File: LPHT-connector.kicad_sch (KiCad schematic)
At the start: 1 part, among them J2 LPHT-04-16-L-RT1-GP

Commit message: minor changes/cleanup
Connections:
- net ET1: now reaches J2.09
- net ET2: now reaches J2.10
- net ET3: now reaches J2.11
- net ET4: now reaches J2.12
- net ET5: now reaches J2.13
- net ET6: now reaches J2.14
- net ET7: now reaches J2.15
- net ET8: now reaches J2.16
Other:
- note added: "This needs to be an "LPHS-04-16-L-VP1""
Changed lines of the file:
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@@
 	(text "9-16 lan\n"
 		(exclude_from_sim no)
-		(at 170.434 85.598 0)
+		(at 182.88 86.106 0)
+		(effects
+			(font
+				(size 1.27 1.27)
+			)
+		)
+	)
+	(text "This needs to be an \"LPHS-04-16-L-VP1\""
+		(exclude_from_sim no)
+		(at 149.86 61.976 0)
 		(effects
 			(font
@@
 	(wire
 		(pts
+			(xy 163.83 85.09) (xy 171.45 85.09)
+		)
+		(stroke
+			(width 0)
+			(type default)
+		)
+	)
+	(wire
+		(pts
 			(xy 138.43 107.95) (xy 138.43 110.49)
 		)
@@
 	(wire
 		(pts
+			(xy 163.83 95.25) (xy 171.45 95.25)
+		)
+		(stroke
+			(width 0)
+			(type default)
+		)
+	)
+	(wire
+		(pts
 			(xy 163.83 115.57) (xy 163.83 118.11)
 		)
@@
 	(wire
 		(pts
+			(xy 163.83 87.63) (xy 171.45 87.63)
+		)
+		(stroke
+			(width 0)
+			(type default)
+		)
+	)
+	(wire
+		(pts
 			(xy 163.83 118.11) (xy 163.83 120.65)
 		)
@@
 	(wire
 		(pts
+			(xy 163.83 90.17) (xy 171.45 90.17)
+		)
+		(stroke
+			(width 0)
+			(type default)
+		)
+	)
+	(wire
+		(pts
 			(xy 127 85.09) (xy 138.43 85.09)
 		)
@@
 	(wire
 		(pts
+			(xy 163.83 77.47) (xy 171.45 77.47)
+		)
+		(stroke
+			(width 0)
+			(type default)
+		)
+	)
+	(wire
+		(pts
 			(xy 138.43 105.41) (xy 138.43 107.95)
 		)
@@
 	(wire
 		(pts
+			(xy 163.83 92.71) (xy 171.45 92.71)
+		)
+		(stroke
+			(width 0)
+			(type default)
+		)
+	)
+	(wire
+		(pts
 			(xy 127 78.74) (xy 138.43 78.74)
 		)
@@
 		(pts
 			(xy 138.43 77.47) (xy 138.43 78.74)
+		)
+		(stroke
+			(width 0)
+			(type default)
+		)
+	)
+	(wire
+		(pts
+			(xy 163.83 82.55) (xy 171.45 82.55)
+		)
+		(stroke
+			(width 0)
+			(type default)
+		)
+	)
+	(wire
+		(pts
+			(xy 163.83 80.01) (xy 171.45 80.01)
 		)
 		(stroke
@@
 		)
 	)
+	(hierarchical_label "ET1"
+		(shape input)
+		(at 171.45 77.47 0)
+		(effects
+			(font
+				(size 1.27 1.27)
+			)
+			(justify left)
+		)
+	)
+	(hierarchical_label "ET4"
+		(shape input)
+		(at 171.45 85.09 0)
+		(effects
+			(font
+				(size 1.27 1.27)
+			)
+			(justify left)
+		)
+	)
+	(hierarchical_label "ET5"
+		(shape input)
+		(at 171.45 87.63 0)
+		(effects
+			(font
+				(size 1.27 1.27)
+			)
+			(justify left)
+		)
+	)
+	(hierarchical_label "ET2"
+		(shape input)
+		(at 171.45 80.01 0)
+		(effects
+			(font
+				(size 1.27 1.27)
+			)
+			(justify left)
+		)
+	)
+	(hierarchical_label "ET8"
+		(shape input)
+		(at 171.45 95.25 0)
+		(effects
+			(font
+				(size 1.27 1.27)
+			)
+			(justify left)
+		)
+	)
+	(hierarchical_label "ET6"
+		(shape input)
+		(at 171.45 90.17 0)
+		(effects
+			(font
+				(size 1.27 1.27)
+			)
+			(justify left)
+		)
+	)
+	(hierarchical_label "ET7"
+		(shape input)
+		(at 171.45 92.71 0)
+		(effects
+			(font
+				(size 1.27 1.27)
+			)
+			(justify left)
+		)
+	)
+	(hierarchical_label "ET3"
+		(shape input)
+		(at 171.45 82.55 0)
+		(effects
+			(font
+				(size 1.27 1.27)
+			)
+			(justify left)
+		)
+	)

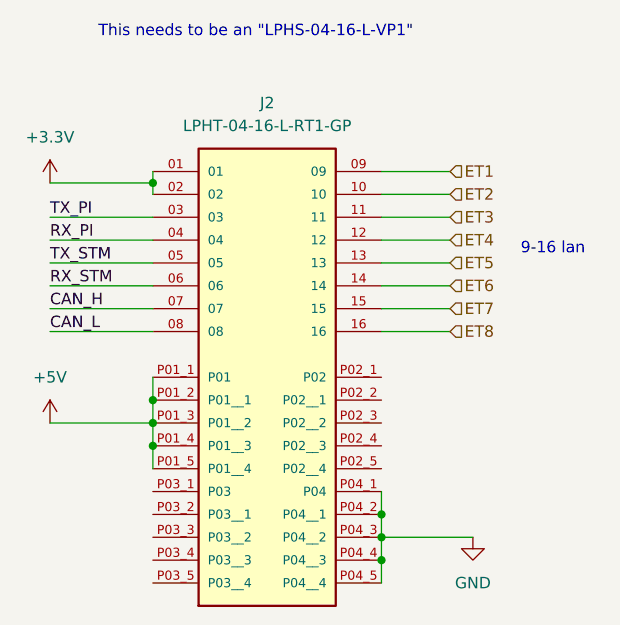
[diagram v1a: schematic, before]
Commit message: Added usb connector
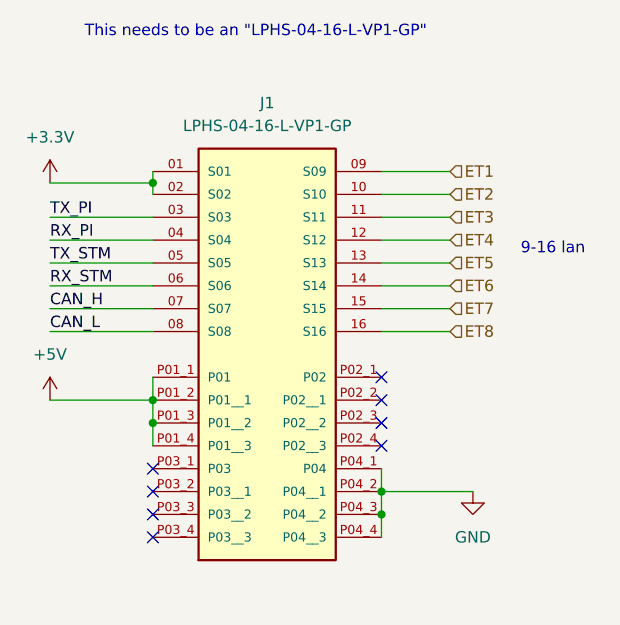
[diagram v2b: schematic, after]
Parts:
- removed J2: LPHT-04-16-L-RT1-GP, dz_con:SAMTEC_LPHT-04-16-X-RT1-GP, symbol #dzdb:s_con/CON-SAMTEC-LPHT-04-16-L-RT1-GP
- added J1: LPHS-04-16-L-VP1-GP, dz_con:SAMTEC_LPHS-04-16-X-VP1-GP, symbol #dzdb:s_con/CON-SAMTEC-LPHS-04-16-L-VP1-GP
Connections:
- net +3.3V: now also J1.01 (S01), J1.02 (S02)
- net +5V: now also J1.P01_1 (P01), J1.P01_2 (P01__1), J1.P01_3 (P01__2), J1.P01_4 (P01__3)
- net CAN_H: now also J1.07 (S07)
- net CAN_L: now also J1.08 (S08)
- net ET1: now also J1.09 (S09)
- net ET2: now also J1.10 (S10)
- net ET3: now also J1.11 (S11)
- net ET4: now also J1.12 (S12)
- net ET5: now also J1.13 (S13)
- net ET6: now also J1.14 (S14)
- net ET7: now also J1.15 (S15)
- net ET8: now also J1.16 (S16)
- net GND: now also J1.P04_1 (P04), J1.P04_2 (P04__1), J1.P04_3 (P04__2), J1.P04_4 (P04__3)
- net RX_PI: now also J1.04 (S04)
- net RX_STM: now also J1.06 (S06)
- net TX_PI: now also J1.03 (S03)
- net TX_STM: now also J1.05 (S05)
- no-connect marks 0 -> 8
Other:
- note added: "This needs to be an "LPHS-04-16-L-VP1-GP""
- note removed: "This needs to be an "LPHS-04-16-L-VP1""

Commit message: Comments (+ new Connector?)
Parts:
- added J3: LPHT-04-16-L-RT1-GP, dz_con:SAMTEC_LPHT-04-16-X-RT1-GP, symbol #dzdb:s_con/CON-SAMTEC-LPHT-04-16-L-RT1-GP
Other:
- note added: "3.3 not needed?"

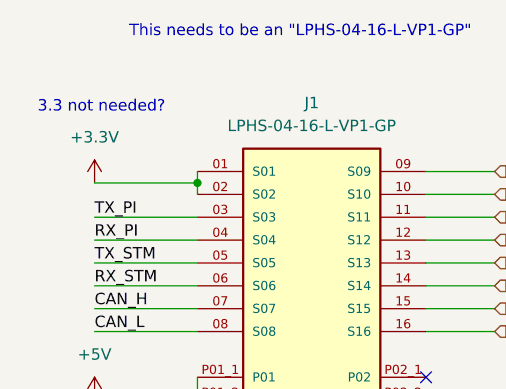
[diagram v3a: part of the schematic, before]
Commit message: multiple changes. fixed some mistakes, added jumper pins for wifi
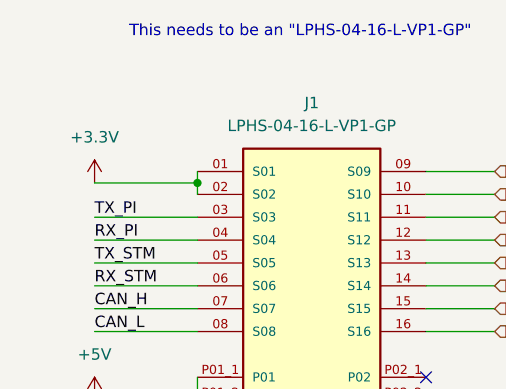
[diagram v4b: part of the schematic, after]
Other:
- note removed: "3.3 not needed?"
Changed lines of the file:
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@@
-		)
-	)
-	(text "3.3 not needed?\n"
-		(exclude_from_sim no)
-		(at 127.762 70.358 0)
-		(effects
-			(font
-				(size 1.27 1.27)
-			)
 		)
 	)

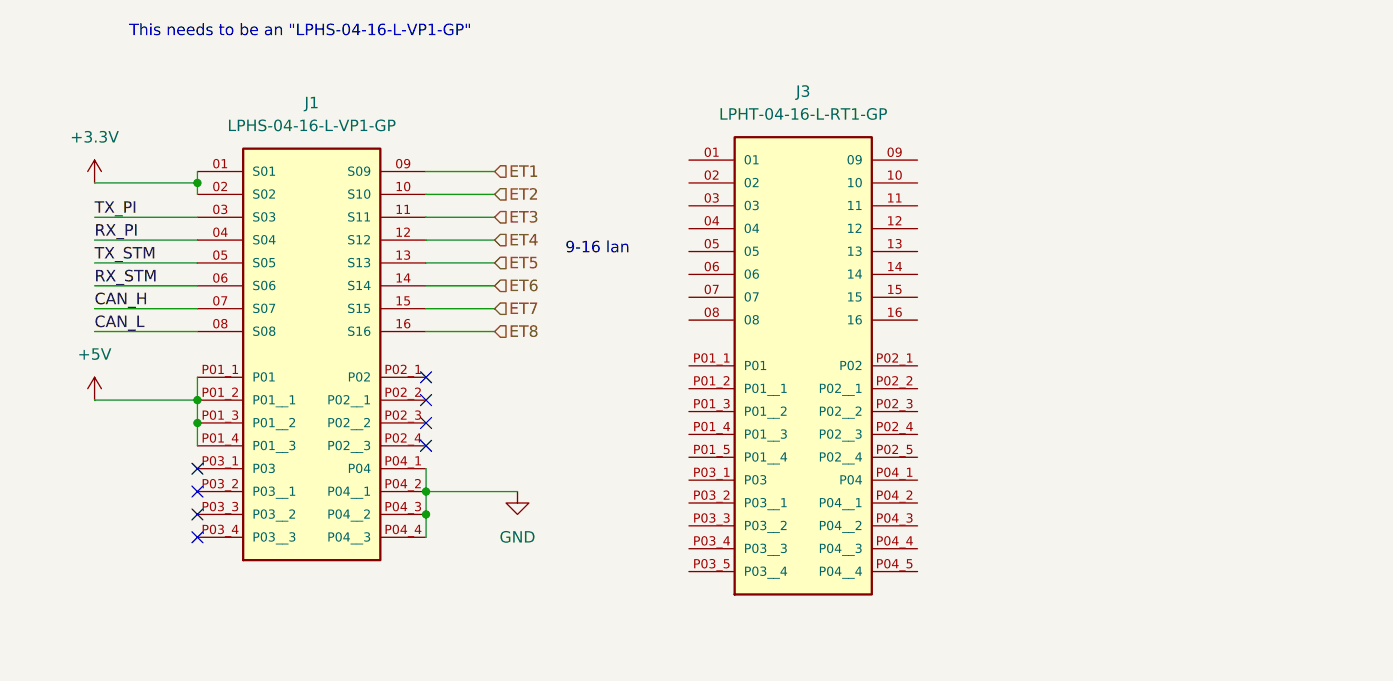
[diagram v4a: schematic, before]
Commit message: connector changes
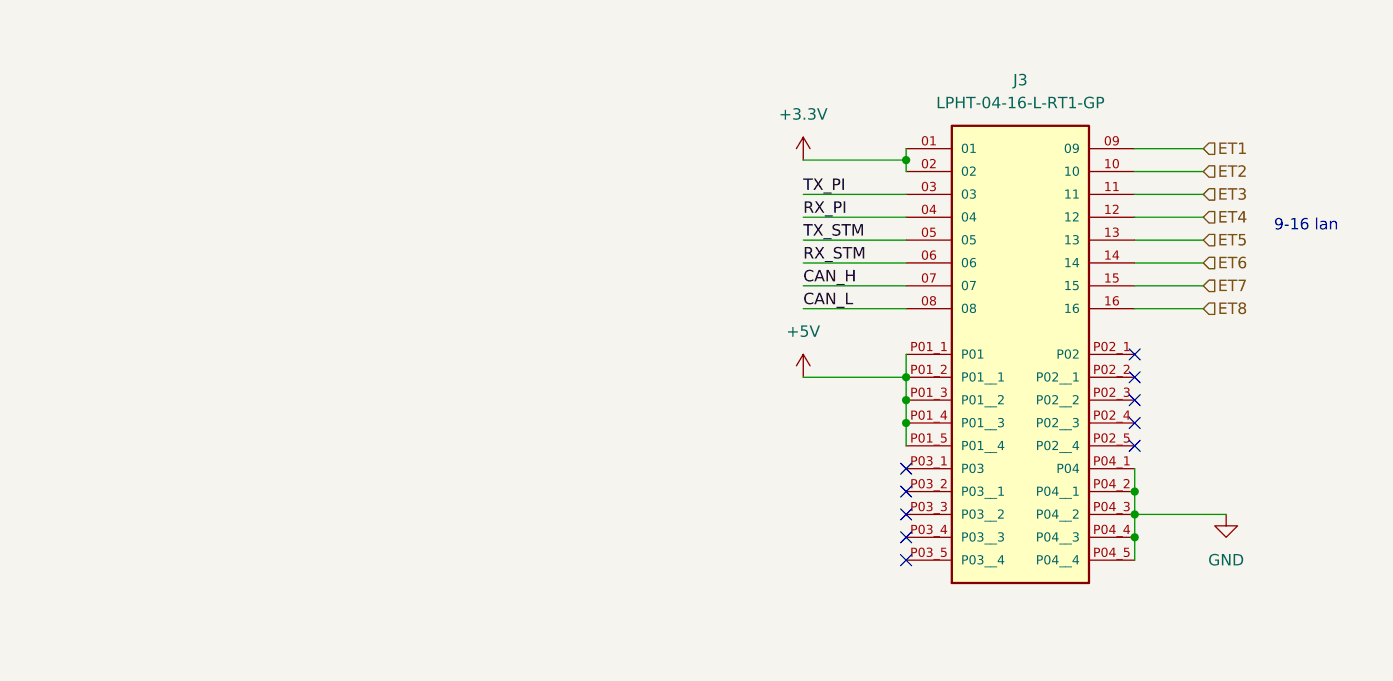
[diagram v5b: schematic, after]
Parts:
- removed J1: LPHS-04-16-L-VP1-GP, dz_con:SAMTEC_LPHS-04-16-X-VP1-GP, symbol #dzdb:s_con/CON-SAMTEC-LPHS-04-16-L-VP1-GP
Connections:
- net +3.3V: now also J3.01, J3.02
- net +5V: now also J3.P01_1 (P01), J3.P01_2 (P01__1), J3.P01_3 (P01__2), J3.P01_4 (P01__3), J3.P01_5 (P01__4)
- net CAN_H: now also J3.07
- net CAN_L: now also J3.08
- net ET1: now also J3.09
- net ET2: now also J3.10
- net ET3: now also J3.11
- net ET4: now also J3.12
- net ET5: now also J3.13
- net ET6: now also J3.14
- net ET7: now also J3.15
- net ET8: now also J3.16
- net GND: now also J3.P04_1 (P04), J3.P04_2 (P04__1), J3.P04_3 (P04__2), J3.P04_4 (P04__3), J3.P04_5 (P04__4)
- net RX_PI: now also J3.04
- net RX_STM: now also J3.06
- net TX_PI: now also J3.03
- net TX_STM: now also J3.05
- no-connect marks 8 -> 10
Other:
- note removed: "This needs to be an "LPHS-04-16-L-VP1-GP""
- moved on the sheet: J3

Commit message: Added Power logic finally. (plus some comments on further improvements)
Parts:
- renumbered J3 to J7
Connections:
- net +3.3V renamed Battery_Out_3.3V
- net +5V renamed Battery_Out_5V
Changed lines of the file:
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@@
+		)
+	)
+	(global_label "Battery_Out_3.3V"
+		(shape output)
+		(at 205.74 76.2 180)
+		(fields_autoplaced yes)
+		(effects
+			(font
+				(size 1.27 1.27)
+			)
+			(justify right)
+		)
+		(property "Intersheetrefs" "${INTERSHEET_REFS}"
+			(at 186.7892 76.2 0)
+			(effects
+				(font
+					(size 1.27 1.27)
+				)
+				(justify right)
+				(hide yes)
+			)
+		)
+	)
+	(global_label "Battery_Out_5V"
+		(shape output)
+		(at 205.74 100.33 180)
+		(fields_autoplaced yes)
+		(effects
+			(font
+				(size 1.27 1.27)
+			)
+			(justify right)
+		)
+		(property "Intersheetrefs" "${INTERSHEET_REFS}"
+			(at 188.6035 100.33 0)
+			(effects
+				(font
+					(size 1.27 1.27)
+				)
+				(justify right)
+				(hide yes)
+			)
 		)
 	)
@@
 			)
 			(justify left)
-		)
-	)
-	(symbol
-		(lib_id "power:+5V")
-		(at 205.74 100.33 0)
-		(unit 1)
-		(exclude_from_sim no)
-		(in_bom yes)
-		(on_board yes)
-		(dnp no)
-		(fields_autoplaced yes)
-		(property "Reference" "#PWR035"
-			(at 205.74 104.14 0)
-			(effects
-				(font
-					(size 1.27 1.27)
-				)
-				(hide yes)
-			)
-		)
-		(property "Value" "+5V"
-			(at 205.74 95.25 0)
-			(effects
-				(font
-					(size 1.27 1.27)
-				)
-			)
-		)
-		(property "Footprint" ""
-			(at 205.74 100.33 0)
-			(effects
-				(font
-					(size 1.27 1.27)
-				)
-				(hide yes)
-			)
-		)
-		(property "Datasheet" ""
-			(at 205.74 100.33 0)
-			(effects
-				(font
-					(size 1.27 1.27)
-				)
-				(hide yes)
-			)
-		)
-		(property "Description" "Power symbol creates a global label with name \"+5V\""
-			(at 205.74 100.33 0)
-			(effects
-				(font
-					(size 1.27 1.27)
-				)
-				(hide yes)
-			)
-		)
-		(pin "1"
-		)
-		(instances
-			(project "nautilus_mainboard"
-				(path "/ce1819b2-f280-40ed-834f-6fe4d12f809d/8ca810bd-6311-4873-a4c4-10e0b1989f7a"
-					(reference "#PWR035")
-					(unit 1)
-				)
-			)
 		)
 	)
@@
 		(dnp no)
 		(fields_autoplaced yes)
-		(property "Reference" "#PWR036"
+		(property "Reference" "#PWR029"
 			(at 252.73 121.92 0)
 			(effects
@@
 			(project "nautilus_mainboard"
 				(path "/ce1819b2-f280-40ed-834f-6fe4d12f809d/8ca810bd-6311-4873-a4c4-10e0b1989f7a"
-					(reference "#PWR036")
-					(unit 1)
-				)
-			)
-		)
-	)
-	(symbol
-		(lib_id "power:+3.3V")
-		(at 205.74 76.2 0)
-		(unit 1)
-		(exclude_from_sim no)
-		(in_bom yes)
-		(on_board yes)
-		(dnp no)
-		(fields_autoplaced yes)
-		(property "Reference" "#PWR034"
-			(at 205.74 80.01 0)
-			(effects
-				(font
-					(size 1.27 1.27)
-				)
-				(hide yes)
-			)
-		)
-		(property "Value" "+3.3V"
-			(at 205.74 71.12 0)
-			(effects
-				(font
-					(size 1.27 1.27)
-				)
-			)
-		)
-		(property "Footprint" ""
-			(at 205.74 76.2 0)
-			(effects
-				(font
-					(size 1.27 1.27)
-				)
-				(hide yes)
-			)
-		)
-		(property "Datasheet" ""
-			(at 205.74 76.2 0)
-			(effects
-				(font
-					(size 1.27 1.27)
-				)
-				(hide yes)
-			)
-		)
-		(property "Description" "Power symbol creates a global label with name \"+3.3V\""
-			(at 205.74 76.2 0)
-			(effects
-				(font
-					(size 1.27 1.27)
-				)
-				(hide yes)
-			)
-		)
-		(pin "1"
-		)
-		(instances
-			(project "nautilus_mainboard"
-				(path "/ce1819b2-f280-40ed-834f-6fe4d12f809d/8ca810bd-6311-4873-a4c4-10e0b1989f7a"
-					(reference "#PWR034")
+					(reference "#PWR029")
 					(unit 1)
 				)
@@
 		(dnp no)
 		(fields_autoplaced yes)
-		(property "Reference" "J3"
+		(property "Reference" "J7"
 			(at 229.87 67.31 0)
 			(effects
@@
 			(project ""
 				(path "/ce1819b2-f280-40ed-834f-6fe4d12f809d/8ca810bd-6311-4873-a4c4-10e0b1989f7a"
-					(reference "J3")
+					(reference "J7")
 					(unit 1)
 				)

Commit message: tried to find some placements for power routing
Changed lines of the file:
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@@
+		)
+	)
+	(text_box "Counterpiece to  LPHS-04-16-L-VP1-GP"
+		(exclude_from_sim no)
+		(at 185.42 60.96 0)
+		(size 83.82 71.12)
+		(margins 0.9525 0.9525 0.9525 0.9525)
+		(stroke
+			(width 0)
+			(type solid)
+		)
+		(fill
+			(type none)
+		)
+		(effects
+			(font
+				(size 1.27 1.27)
+			)
+			(justify left top)
 		)
 	)
@@
 	)
 	(image
-		(at 154.94 96.52)
+		(at 139.7 91.44)
 		(scale 0.431936)
 		(data "iVBORw0KGgoAAAANSUhEUgAAAhEAAANTCAIAAACfG9iWAAAAA3NCSVQICAjb4U/gAAAACXBIWXMA"

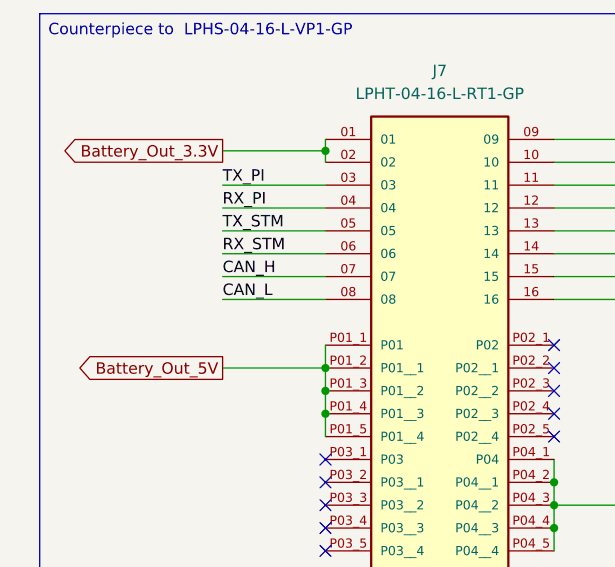
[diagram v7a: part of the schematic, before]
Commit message: routed the CAN
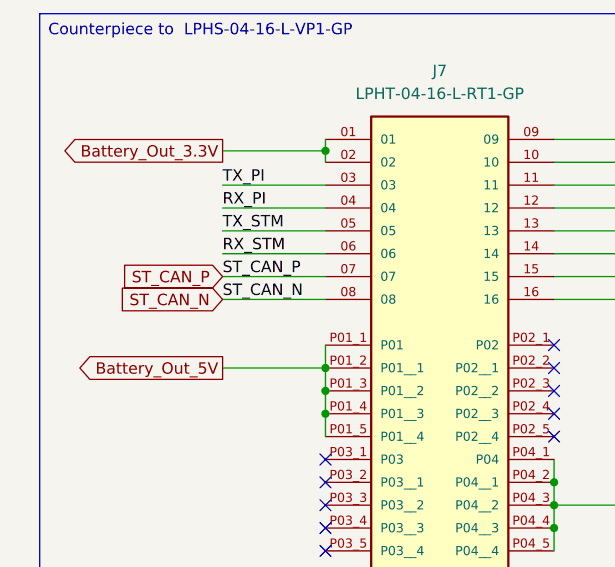
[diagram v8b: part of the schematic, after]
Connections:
- net CAN_H renamed ST_CAN_P
- net CAN_L renamed ST_CAN_N
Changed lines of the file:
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@@
 		)
 	)
-	(label "CAN_H"
+	(label "ST_CAN_P"
 		(at 205.74 90.17 0)
 		(effects
@@
 		)
 	)
-	(label "CAN_L"
+	(label "ST_CAN_N"
 		(at 205.74 92.71 0)
 		(effects
@@
 		)
 	)
+	(global_label "ST_CAN_N"
+		(shape input)
+		(at 205.74 92.71 180)
+		(fields_autoplaced yes)
+		(effects
+			(font
+				(size 1.27 1.27)
+			)
+			(justify right)
+		)
+		(property "Intersheetrefs" "${INTERSHEET_REFS}"
+			(at 193.6229 92.71 0)
+			(effects
+				(font
+					(size 1.27 1.27)
+				)
+				(justify right)
+				(hide yes)
+			)
+		)
+	)
 	(global_label "Battery_Out_5V"
 		(shape output)
@@
 			(effects
 				(font
+					(size 1.27 1.27)
+				)
+				(justify right)
+				(hide yes)
+			)
+		)
+	)
+	(global_label "ST_CAN_P"
+		(shape input)
+		(at 205.74 90.17 180)
+		(fields_autoplaced yes)
+		(effects
+			(font
+				(size 1.27 1.27)
+			)
+			(justify right)
+		)
+		(property "Intersheetrefs" "${INTERSHEET_REFS}"
+			(at 193.6834 90.17 0)
+			(effects
+				(font
